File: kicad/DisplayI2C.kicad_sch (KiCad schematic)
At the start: 39 parts

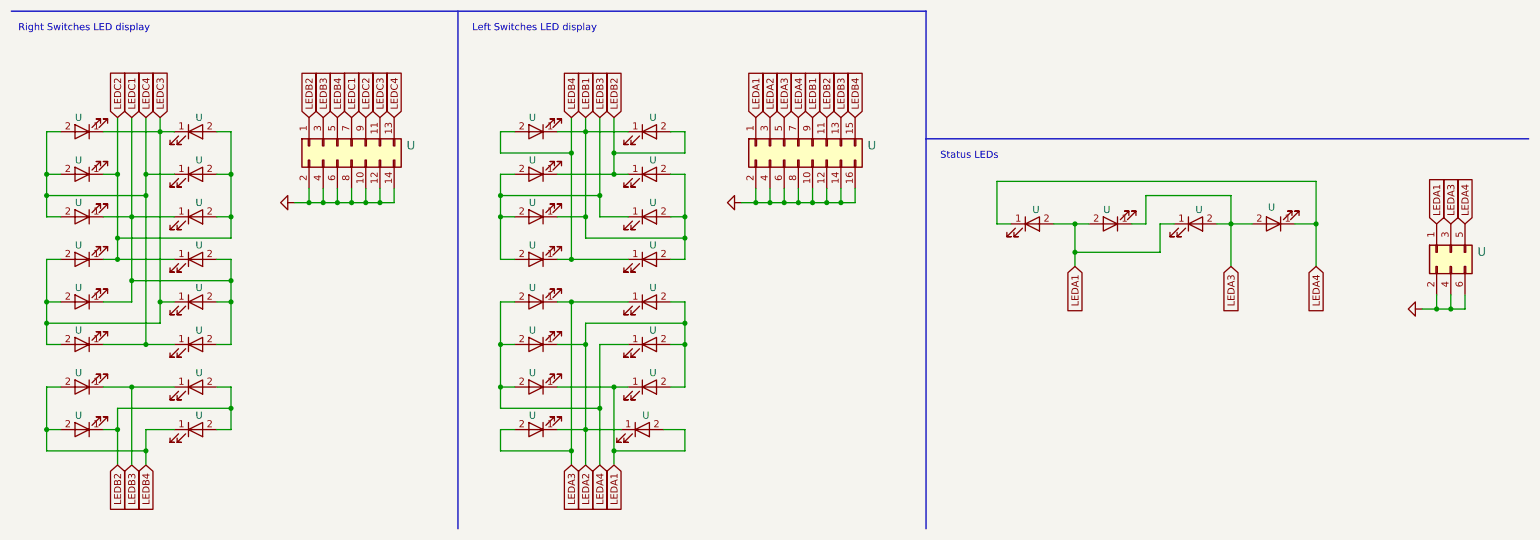
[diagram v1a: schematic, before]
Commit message: Adding PIB USB BRIDGE UML state diagrams - WIP
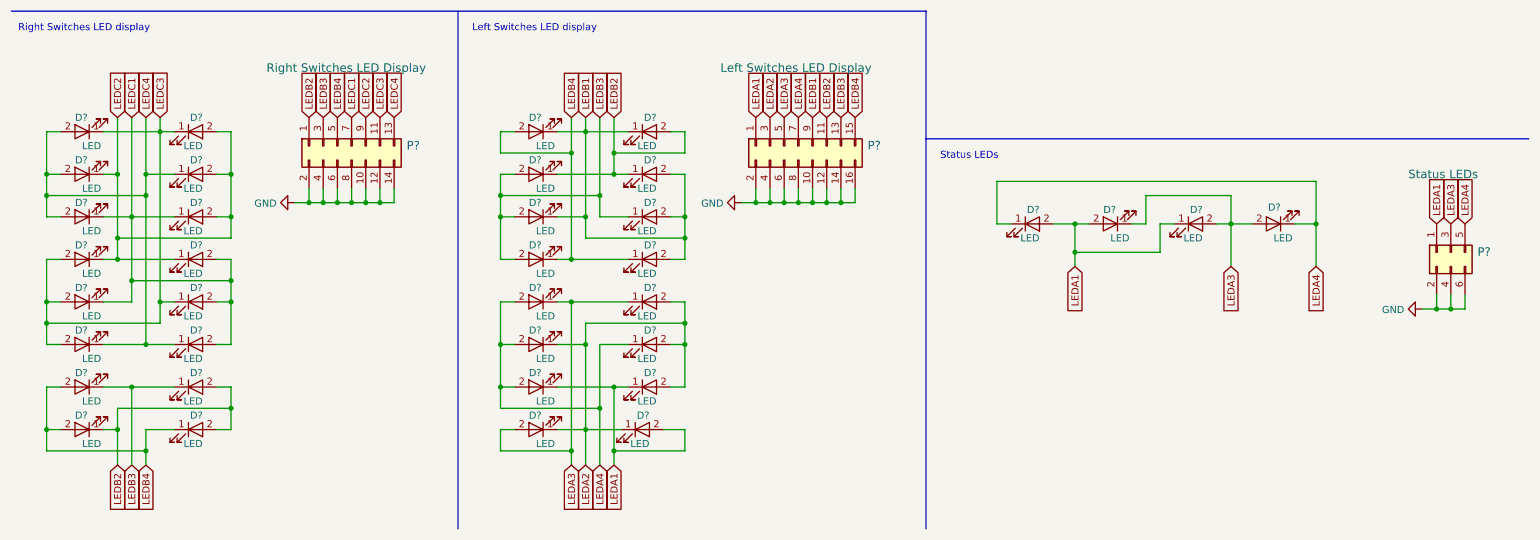
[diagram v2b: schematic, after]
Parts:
- D? (x36): renamed from U; value (none) -> LED
- P?: renamed from U; value (none) -> Right Switches LED Display
- P?: renamed from U; value (none) -> Left Switches LED Display
- P?: renamed from U; value (none) -> Status LEDs

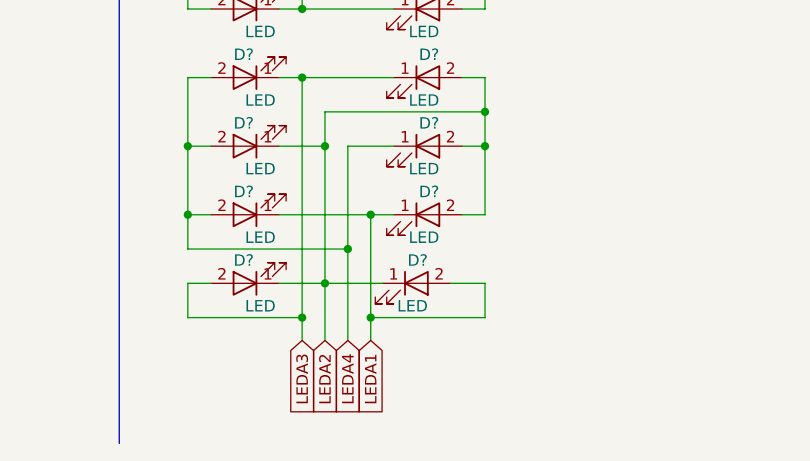
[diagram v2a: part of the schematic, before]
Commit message: Using MAX6969/MAX6971 SPI LEDs driver
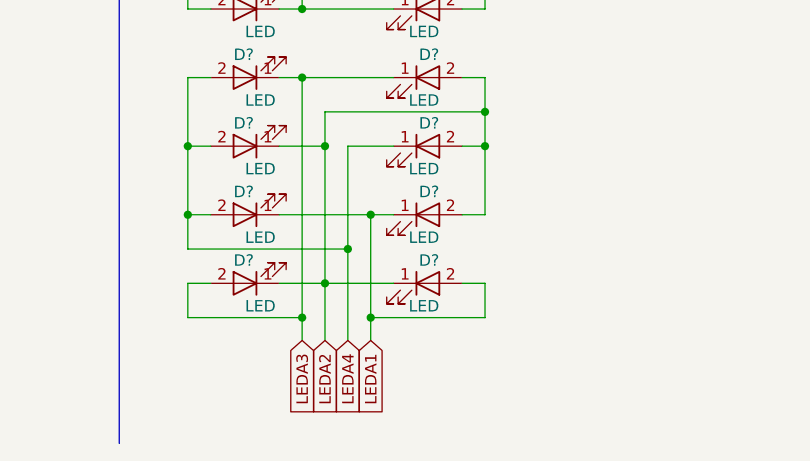
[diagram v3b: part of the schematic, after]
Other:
- moved on the sheet: D?
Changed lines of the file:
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@@
     (stroke (width 0) (type default))
   )
-  (wire (pts (xy 129.54 180.34) (xy 133.35 180.34))
+  (wire (pts (xy 130.81 180.34) (xy 133.35 180.34))
     (stroke (width 0) (type default))
   )
@@
     (stroke (width 0) (type default))
   )
-  (wire (pts (xy 115.57 180.34) (xy 121.92 180.34))
+  (wire (pts (xy 115.57 180.34) (xy 123.19 180.34))
     (stroke (width 0) (type default))
   )
@@
     )
   )
-  (symbol (lib_id "device:LED") (at 125.73 180.34 0) (unit 1)
-    (in_bom yes) (on_board yes) (dnp no)
-    (property "Reference" "D?" (at 127 177.8 0)
-      (effects (font (size 1.27 1.27)) (justify right))
-    )
-    (property "Value" "LED" (at 127 182.88 0)
-      (effects (font (size 1.27 1.27)) (justify right))
-    )
-    (property "Footprint" "" (at 125.73 180.34 0)
-      (effects (font (size 1.27 1.27)) hide)
-    )
-    (property "Datasheet" "" (at 125.73 180.34 0)
-      (effects (font (size 1.27 1.27)) hide)
-    )
+  (symbol (lib_id "device:LED") (at 127 180.34 0) (unit 1)
+    (in_bom yes) (on_board yes) (dnp no)
+    (property "Reference" "D?" (at 128.27 177.8 0)
+      (effects (font (size 1.27 1.27)) (justify right))
+    )
+    (property "Value" "LED" (at 128.27 182.88 0)
+      (effects (font (size 1.27 1.27)) (justify right))
+    )
+    (property "Footprint" "" (at 127 180.34 0)
+      (effects (font (size 1.27 1.27)) hide)
+    )
+    (property "Datasheet" "" (at 127 180.34 0)
+      (effects (font (size 1.27 1.27)) hide)
+    )
